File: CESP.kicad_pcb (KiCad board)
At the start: 2 copper layers, 50.8 x 25.4 mm, 19 parts, among them K1 CONN_3, P1 CONN_7, U1 7555, U2 LM741, U3 7805-REG

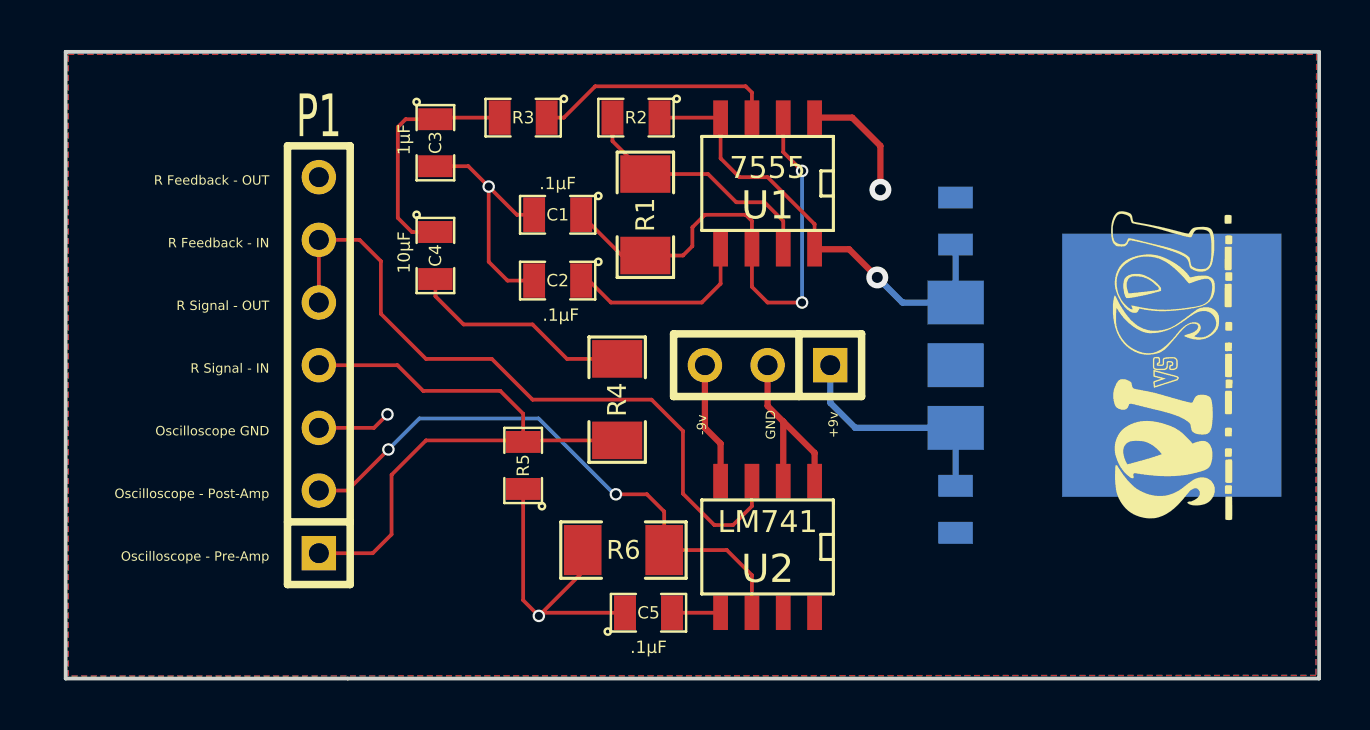
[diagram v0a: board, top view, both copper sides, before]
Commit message: Added TSSOP, MSOP and regenerated gerbers...
1. TSSOP 555 blinky circuit added with teeny components to backside
copper.
2. MSOP pads added to back, not connected to anything.
3. Gerbers updated.  Trial run through OshPark for validation
successful.
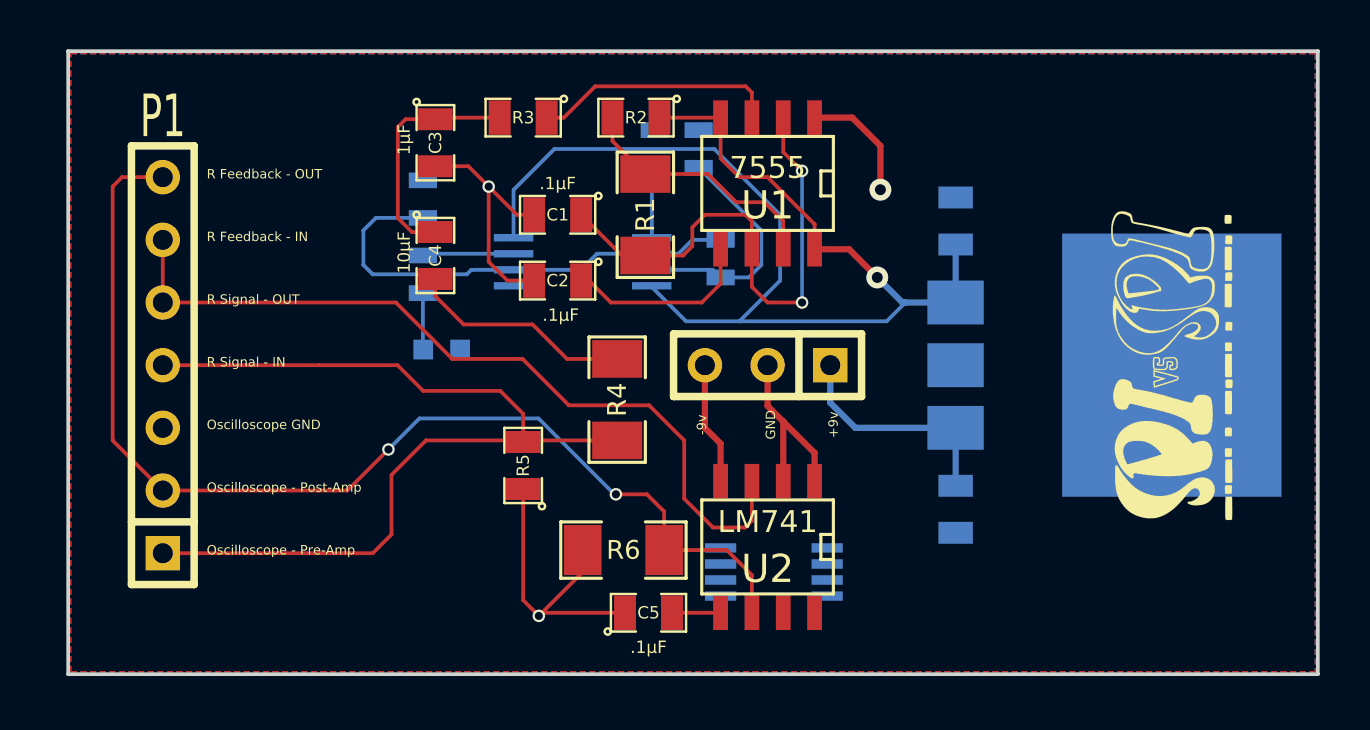
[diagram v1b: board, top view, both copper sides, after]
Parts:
- added C8: 10µF, SM0603_Capa, B.Cu at (201.8, 134.1)
- added C9: .1µF, SM0603_Capa, B.Cu at (211.2, 132.1)
- added D1: LED, LED-0603, B.Cu at (202.6, 140.2)
- added R7: 4K7, SM0603, B.Cu at (213.0, 132.1)
- added R8: 180K, SM0603, B.Cu at (213.9, 136.5)
- added R9: 330, SM0603, B.Cu at (201.8, 137.2)
- added U4: 7555, TSSOP-8, B.Cu at (208.3, 136.7)
- added U5: TL082, MSOP_8, B.Cu at (216.0, 149.2)
- moved P1 6.32 mm to (191.3, 140.8)
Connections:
- P1 pad 2: N-000008 -> N-0000027
- P1 pad 7: VCC -> N-0000027
- R6 pad 2: N-000008 -> N-0000027
- U2 pad 6: N-000008 -> N-0000027
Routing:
- net N-0000027: track 0.00 -> 45.5 mm, vias 0 -> 2
- net N-0000029: track 19.0 -> 49.8 mm
- net N-000008: track 23.8 -> 2.89 mm, vias 2 -> 0
- net N-0000020: track 0.00 -> 19.2 mm
- net N-000001: track 25.7 -> 38.3 mm
- net N-0000019: track 0.00 -> 9.77 mm
- net N-000002: track 28.9 -> 33.3 mm
- net N-000006: track 0.00 -> 3.71 mm
- net GND: track 38.2 -> 35.2 mm, vias 4 -> 3
- net N-000007: track 0.00 -> 2.29 mm
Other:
- board size 50.8 x 25.4 mm -> 50.6 x 25.2 mm
- board text added: "Little Blinky"
- board text added: "MSOP-8 Practice Pad"
